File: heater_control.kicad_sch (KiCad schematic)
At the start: 14 parts, among them J11 Conn_02x02_Counter_Clockwise, J12 Conn_02x04_Counter_Clockwise

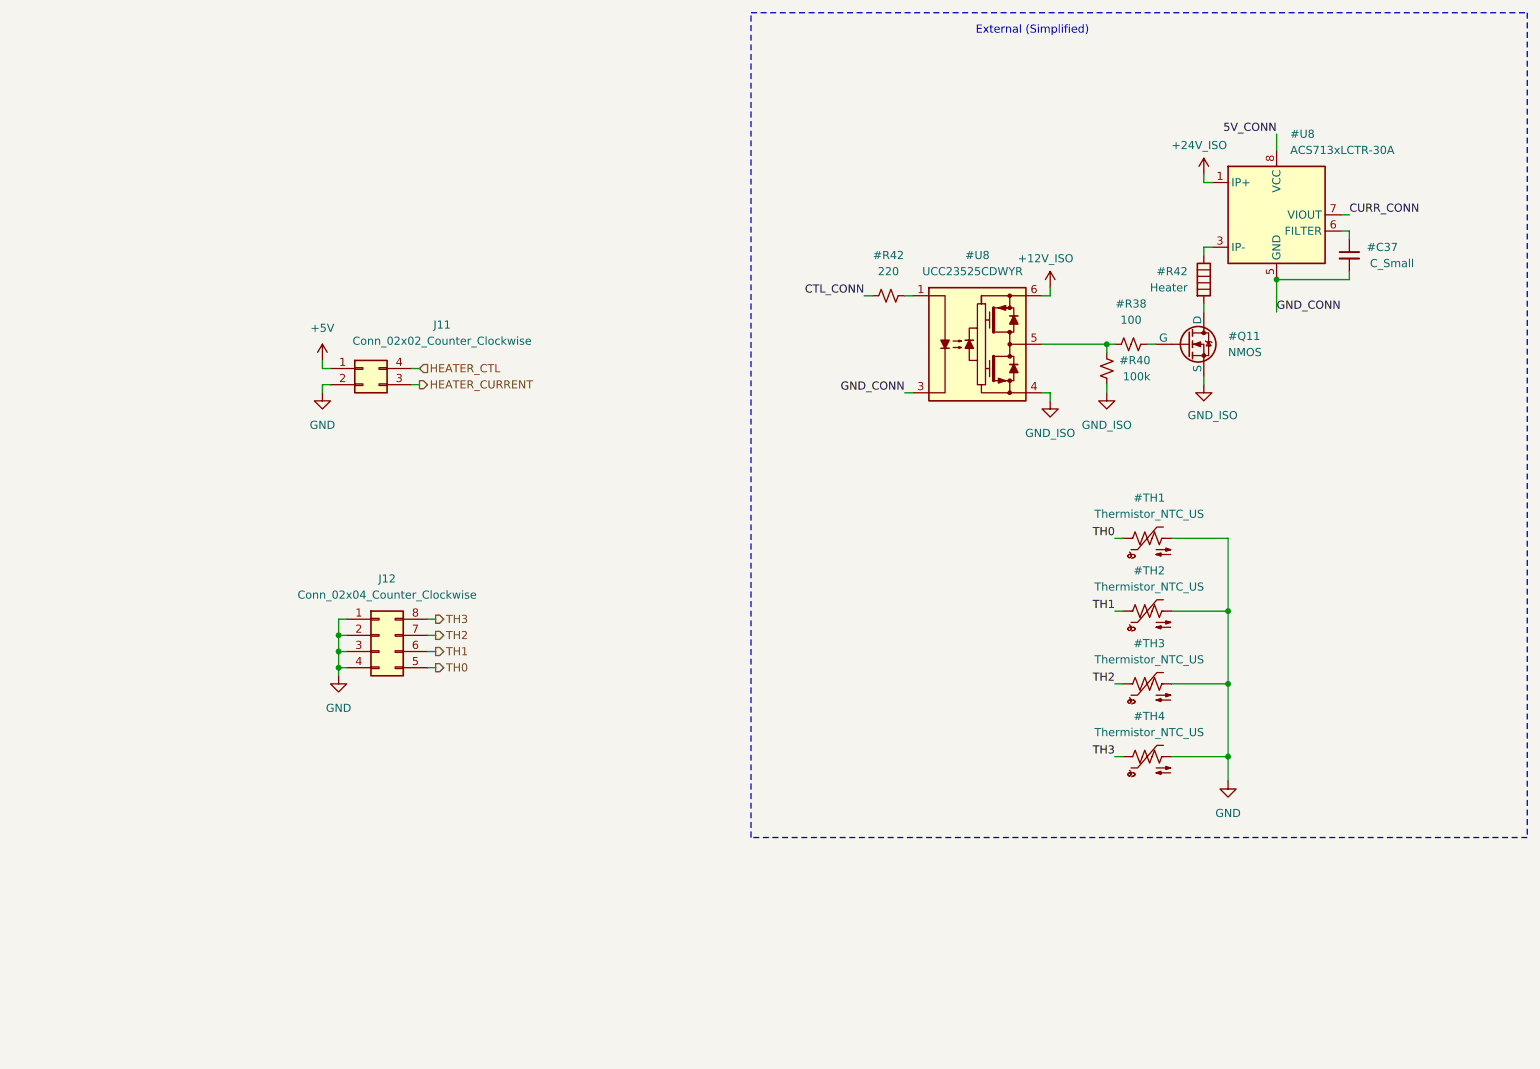
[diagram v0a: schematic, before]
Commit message: add heater power regulation for fet switching
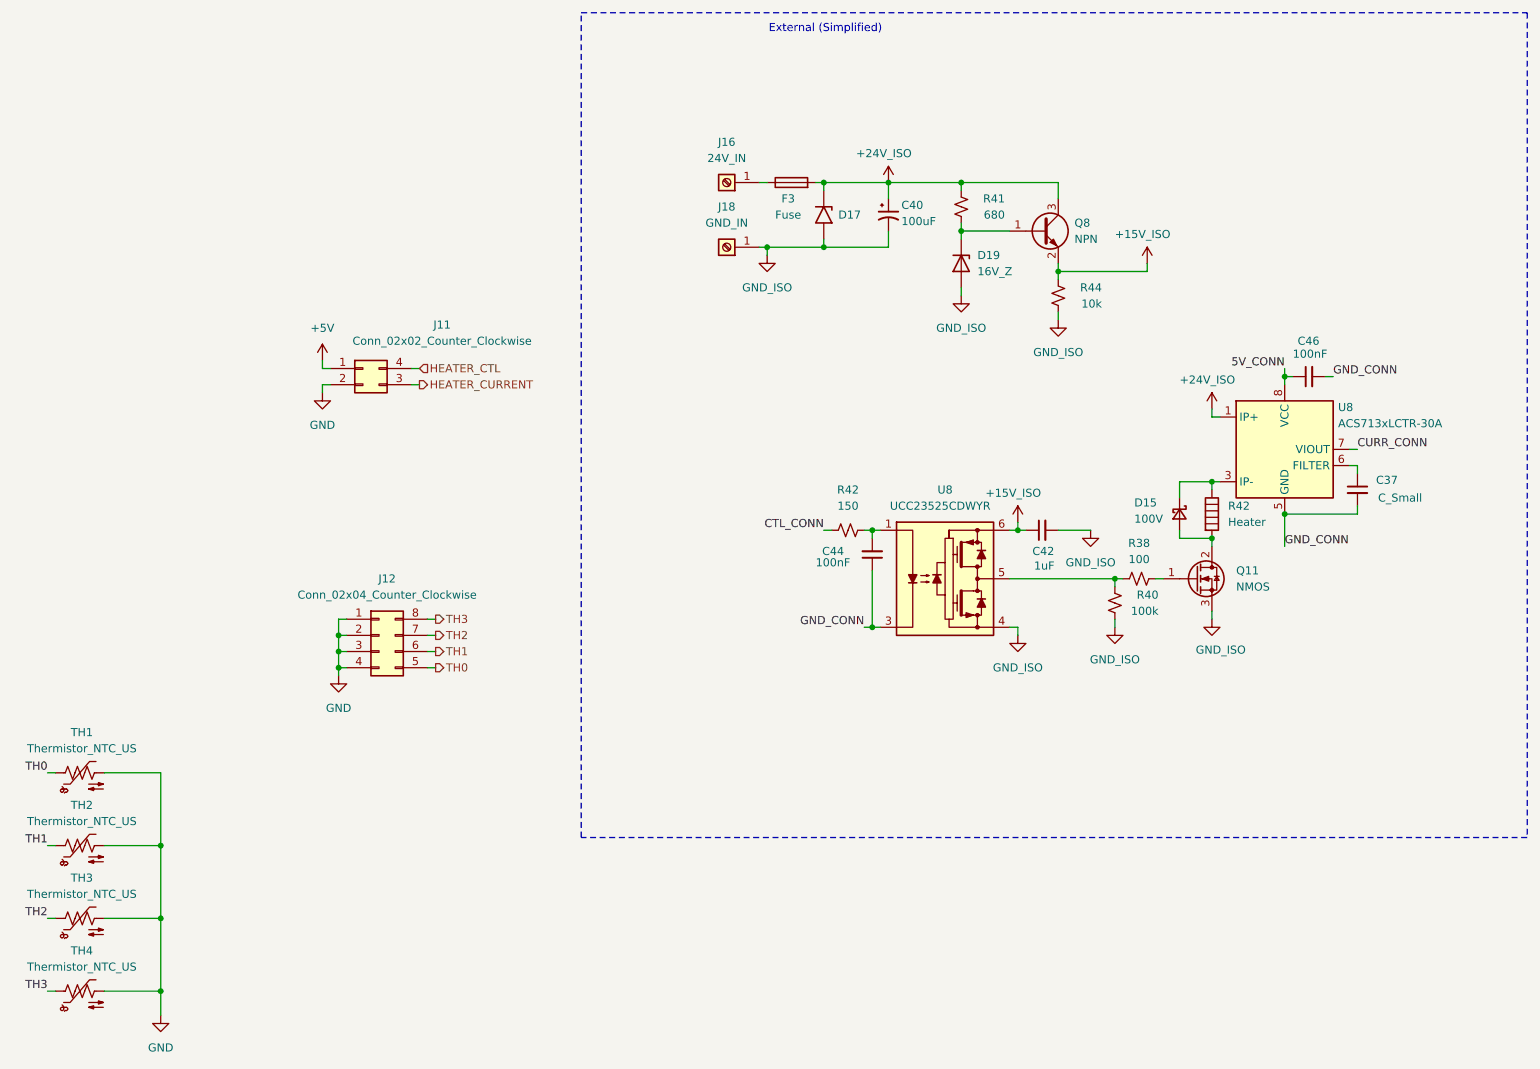
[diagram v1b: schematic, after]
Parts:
- added C40: 100uF, Capacitor_SMD:CP_Elec_10x10, symbol Device:C_Polarized_Small_US
- added C42: 1uF, Capacitor_SMD:C_0805_2012Metric_Pad1.18x1.45mm_HandSolder, symbol Device:C_Small
- added C44, C46: 100nF, Capacitor_SMD:C_0805_2012Metric_Pad1.18x1.45mm_HandSolder, symbol Device:C_Small
- added D15: 100V, Diode_SMD:D_SMA_Handsoldering, symbol Device:D_Schottky_Small
- added D17: SMCJ26A-13-F, Diode_SMD:D_SMC, symbol Diode:1.5SMCxxA
- added D19: 16V_Z, Diode_SMD:D_SOD-123, symbol Device:D_Zener
- added F3: Fuse, Fuse:Fuseholder_Blade_Mini_Keystone_3568, symbol Device:Fuse
- added J16: 24V_IN, symbol Connector:Screw_Terminal_01x01
- added J18: GND_IN, symbol Connector:Screw_Terminal_01x01
- added Q8: NPN, Package_TO_SOT_SMD:SOT-23_Handsoldering, symbol Transistor_BJT:Q_NPN_BEC
- added R41: 680, Resistor_SMD:R_0805_2012Metric_Pad1.20x1.40mm_HandSolder, symbol Device:R_Small_US
- added R44: 10k, Resistor_SMD:R_0805_2012Metric_Pad1.20x1.40mm_HandSolder, symbol Device:R_Small_US
- C37: renamed from #C37; footprint (none) -> Capacitor_SMD:C_0805_2012Metric_Pad1.18x1.45mm_HandSolder
- Q11: renamed from #Q11; footprint (none) -> Package_TO_SOT_SMD:TO-252-2; symbol Simulation_SPICE:NMOS -> Transistor_FET:Q_NMOS_GDS; MPN (none) -> STD130N6F7
- R38: renamed from #R38; footprint (none) -> Resistor_SMD:R_0805_2012Metric_Pad1.20x1.40mm_HandSolder
- R40: renamed from #R40; footprint (none) -> Resistor_SMD:R_0805_2012Metric_Pad1.20x1.40mm_HandSolder
- R42: renamed from #R42; value 220 -> 150; footprint (none) -> Resistor_SMD:R_0805_2012Metric_Pad1.20x1.40mm_HandSolder
- U8: renamed from #U8; MPN (none) -> ACS713ELCTR-30A-T
- renumbered #R42 to R42, #TH1 to TH1, #TH2 to TH2, #TH3 to TH3, #TH4 to TH4, #U8 to U8
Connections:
- net +24V_ISO: now also C40.1, D17.1 (A1), F3.2, Q8.3 (C), R41.2
- net 5V_CONN: now also C46.1
- net GND_CONN: now also C44.1, C46.2
- net GND_ISO: now also C40.2, C42.2, D17.2 (A2), D19.2 (A), J18.1 (Pin_1), R44.1
- net at R42.1, U8.3 (IP-), U8.4 (IP-): now also D15.1 (K)
- net at R42.1, U8.1 (A): now also C44.2
- net at R38.2: now also Q11.1 (G); no longer Q11.2 (G)
- net at R42.2: now also Q11.2 (D), D15.2 (A); no longer Q11.1 (D)
- net +12V_ISO renamed +15V_ISO
- net +15V_ISO: now also C42.1, Q8.2 (E), R44.2
- new net: F3.1, J16.1 (Pin_1)
- new net: D19.1 (K), Q8.1 (B), R41.1
